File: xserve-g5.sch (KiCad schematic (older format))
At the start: 17 parts, among them J1 SATA_Backplane_PWR, J10 FAN5_PWM, J11 FAN6_PWM, J12 FAN7_PWM, J2 FAN_LEFT, J3 FAN_RIGHT, J4 PWR_L, J5 PWR_R, J6 FAN1_PWM, J7 FAN2_PWM, J8 FAN3_PWM, J9 FAN4_PWM

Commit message: updates
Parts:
- added J13: Front Panel, Connector_PinHeader_1.27mm:PinHeader_2x17_P1.27mm_Vertical, symbol Connector_Generic:Conn_02x17_Odd_Even
- added U1: WeMos_D1_mini, Module:WEMOS_D1_mini_light, symbol MCU_Module:WeMos_D1_mini
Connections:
- net +5V: now also J13.26 (Pin_26), J13.28 (Pin_28), J13.30 (Pin_30), J13.32 (Pin_32), J13.34 (Pin_34), U1.9 (5V)
- net GND: now also J13.1 (Pin_1), J13.11 (Pin_11), J13.17 (Pin_17), J13.25 (Pin_25), J13.27 (Pin_27), J13.29 (Pin_29), J13.31 (Pin_31), J13.33 (Pin_33), J13.7 (Pin_7), U1.10 (GND)
- new net +3V3: U1.8 (3V3)
- new net CLED_RCLK: J13.10 (Pin_10)
- new net CLED_SER: J13.12 (Pin_12)
- new net CLED_SRCLK: J13.8 (Pin_8)
- new net CLED_SRCLR_n: J13.13 (Pin_13)
- new net CLED_VCC: J13.4 (Pin_4)
- new net LANA_LED: J13.19 (Pin_19)
- new net LANB_LED: J13.18 (Pin_18)
- new net PWR_LED: J13.5 (Pin_5)
- new net PWR_SW: J13.3 (Pin_3)
- new net Q19: J13.2 (Pin_2)
- new net SRVID_LED: J13.15 (Pin_15)
- new net SRVID_SW: J13.6 (Pin_6)
- new net U6_??: J13.20 (Pin_20)
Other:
- note added: "Guessed"
- note added: "apply GND"
- note added: "apply Voltage"
- note added: "to GND"
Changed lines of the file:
@@
 Wire Notes Line
 	4850 550  550  550
+$Comp
+L power:GND #PWR0103
+U 1 1 5F39D41C
+P 6700 2300
+F 0 "#PWR0103" H 6700 2050 50  0001 C CNN
+F 1 "GND" H 6705 2127 50  0000 C CNN
+F 2 "" H 6700 2300 50  0001 C CNN
+F 3 "" H 6700 2300 50  0001 C CNN
+	1    6700 2300
+	0    1    1    0
+$EndComp
+$Comp
+L Connector_Generic:Conn_02x17_Odd_Even J13
+U 1 1 5F3A8D6B
+P 7000 1700
+F 0 "J13" H 7050 2717 50  0000 C CNN
+F 1 "Front Panel" H 7050 2626 50  0000 C CNN
+F 2 "Connector_PinHeader_1.27mm:PinHeader_2x17_P1.27mm_Vertical" H 7000 1700 50  0001 C CNN
+F 3 "~" H 7000 1700 50  0001 C CNN
+F 4 "Harwin M50-3551742" H 7000 1700 50  0001 C CNN "Part"
+	1    7000 1700
+	1    0    0    -1
+$EndComp
+$Comp
+L MCU_Module:WeMos_D1_mini U1
+U 1 1 5F3B1E0C
+P 9600 1650
+F 0 "U1" H 9600 669 50  0000 C CNN
+F 1 "WeMos_D1_mini" H 9600 760 50  0000 C CNN
+F 2 "Module:WEMOS_D1_mini_light" H 9600 500 50  0001 C CNN
+F 3 "https://wiki.wemos.cc/products:d1:d1_mini#documentation" H 7750 500 50  0001 C CNN
+	1    9600 1650
+	-1   0    0    1
+$EndComp
+$Comp
+L power:GND #PWR0121
+U 1 1 5F3C5F82
+P 9600 850
+F 0 "#PWR0121" H 9600 600 50  0001 C CNN
+F 1 "GND" H 9605 677 50  0000 C CNN
+F 2 "" H 9600 850 50  0001 C CNN
+F 3 "" H 9600 850 50  0001 C CNN
+	1    9600 850
+	0    -1   -1   0
+$EndComp
+Text GLabel 6800 1100 0    50   Input ~ 0
+PWR_LED
+Wire Wire Line
+	6800 2100 6800 2200
+Wire Wire Line
+	6800 2200 6800 2300
+Connection ~ 6800 2200
+Wire Wire Line
+	6800 2300 6800 2400
+Connection ~ 6800 2300
+Connection ~ 6800 2400
+Wire Wire Line
+	6800 2400 6800 2500
+Wire Wire Line
+	6700 2300 6800 2300
+Text GLabel 7300 1400 2    50   Input ~ 0
+CLED_SER
+Text GLabel 7300 1000 2    50   Input ~ 0
+CLED_VCC
+$Comp
+L power:GND #PWR?
+U 1 1 5F3CE2DC
+P 6800 900
+F 0 "#PWR?" H 6800 650 50  0001 C CNN
+F 1 "GND" H 6805 727 50  0000 C CNN
+F 2 "" H 6800 900 50  0001 C CNN
+F 3 "" H 6800 900 50  0001 C CNN
+	1    6800 900
+	0    1    1    0
+$EndComp
+$Comp
+L power:GND #PWR?
+U 1 1 5F3CEC27
+P 6800 1200
+F 0 "#PWR?" H 6800 950 50  0001 C CNN
+F 1 "GND" H 6805 1027 50  0000 C CNN
+F 2 "" H 6800 1200 50  0001 C CNN
+F 3 "" H 6800 1200 50  0001 C CNN
+	1    6800 1200
+	0    1    1    0
+$EndComp
+$Comp
+L power:GND #PWR?
+U 1 1 5F3CEED3
+P 6800 1400
+F 0 "#PWR?" H 6800 1150 50  0001 C CNN
+F 1 "GND" H 6805 1227 50  0000 C CNN
+F 2 "" H 6800 1400 50  0001 C CNN
+F 3 "" H 6800 1400 50  0001 C CNN
+	1    6800 1400
+	0    1    1    0
+$EndComp
+$Comp
+L power:GND #PWR?
+U 1 1 5F3CF6D7
+P 6800 1700
+F 0 "#PWR?" H 6800 1450 50  0001 C CNN
+F 1 "GND" H 6805 1527 50  0000 C CNN
+F 2 "" H 6800 1700 50  0001 C CNN
+F 3 "" H 6800 1700 50  0001 C CNN
+	1    6800 1700
+	0    1    1    0
+$EndComp
+Text GLabel 7300 1300 2    50   Input ~ 0
+CLED_RCLK
+Text GLabel 7300 1200 2    50   Input ~ 0
+CLED_SRCLK
+Text GLabel 6800 1500 0    50   Input ~ 0
+CLED_SRCLR_n
+Wire Wire Line
+	7300 2100 7300 2200
+Wire Wire Line
+	7300 2200 7300 2300
+Connection ~ 7300 2200
+Wire Wire Line
+	7300 2300 7300 2400
+Connection ~ 7300 2300
+Wire Wire Line
+	7300 2400 7300 2500
+Connection ~ 7300 2400
+$Comp
+L power:+5V #PWR?
+U 1 1 5F3D4B59
+P 7300 2300
+F 0 "#PWR?" H 7300 2150 50  0001 C CNN
+F 1 "+5V" V 7315 2428 50  0000 L CNN
+F 2 "" H 7300 2300 50  0001 C CNN
+F 3 "" H 7300 2300 50  0001 C CNN
+	1    7300 2300
+	0    1    1    0
+$EndComp
+$Comp
+L power:+5V #PWR?
+U 1 1 5F3D5D72
+P 9700 2450
+F 0 "#PWR?" H 9700 2300 50  0001 C CNN
+F 1 "+5V" H 9715 2623 50  0000 C CNN
+F 2 "" H 9700 2450 50  0001 C CNN
+F 3 "" H 9700 2450 50  0001 C CNN
+	1    9700 2450
+	-1   0    0    1
+$EndComp
+Text Notes 7600 2350 0    50   ~ 0
+Guessed
+Text GLabel 6800 1000 0    50   Input ~ 0
+PWR_SW
+Text Notes 6150 1050 0    50   ~ 0
+to GND
+Text GLabel 7300 1100 2    50   Input ~ 0
+SRVID_SW
+Text Notes 7750 1100 0    50   ~ 0
+to GND
+Text GLabel 6800 1600 0    50   Input ~ 0
+SRVID_LED
+Text Notes 5900 1150 0    50   ~ 0
+apply Voltage
+Text Notes 5950 1650 0    50   ~ 0
+apply GND
+Text GLabel 6800 1800 0    50   Input ~ 0
+LANA_LED
+Text GLabel 7300 1700 2    50   Input ~ 0
+LANB_LED
+$Comp
+L power:+3.3V #PWR?
+U 1 1 5F3DAB15
+P 9500 2450
+F 0 "#PWR?" H 9500 2300 50  0001 C CNN
+F 1 "+3.3V" H 9515 2623 50  0000 C CNN
+F 2 "" H 9500 2450 50  0001 C CNN
+F 3 "" H 9500 2450 50  0001 C CNN
+	1    9500 2450
+	-1   0    0    1
+$EndComp
+Text GLabel 7300 900  2    50   Input ~ 0
+Q19
+Text GLabel 7300 1800 2    50   Input ~ 0
+U6_??
 $EndSCHEMATC

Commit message: update
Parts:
- added J14: SYSTEM_PINS, Connector_PinHeader_2.54mm:PinHeader_1x06_P2.54mm_Horizontal, symbol Connector_Generic:Conn_01x06
- added J15: CLED_VCC, Connector_PinHeader_2.54mm:PinHeader_1x03_P2.54mm_Vertical, symbol Connector_Generic:Conn_01x03
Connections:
- net CLED_VCC is gone; now on net CLED_SRCLR_n: J13.4 (Pin_4)
- net U6_?? is gone; now on net CLED_SRCLR_n: J13.20 (Pin_20)
- net +12V: no longer J3.10 (Pin_10), J3.8 (Pin_8), J5.1 (Pin_1)
- net +3V3: now also J15.1 (Pin_1)
- net +5V: no longer J13.26 (Pin_26), J13.28 (Pin_28), J13.30 (Pin_30), J13.32 (Pin_32), J13.34 (Pin_34), U1.9 (5V)
- net CLED_RCLK: now also U1.6 (MOSI/D7)
- net CLED_SER: now also U1.5 (MISO/D6)
- net CLED_SRCLK: now also U1.4 (SCK/D5)
- net CLED_SRCLR_n: now also J13.14 (Pin_14), J13.9 (Pin_9), J15.2 (Pin_2)
- net LANA_LED: now also J14.5 (Pin_5)
- net LANB_LED: now also J14.6 (Pin_6)
- net PWR_LED: now also J14.1 (Pin_1)
- net PWR_SW: now also J14.2 (Pin_2)
- net SRVID_LED: now also J14.3 (Pin_3)
- net SRVID_SW: now also J14.4 (Pin_4)
- net Q13: now reaches J13.22 (Pin_22)
- new net +12VA: J3.10 (Pin_10), J3.8 (Pin_8), J5.1 (Pin_1)
- new net +5VA: J13.26 (Pin_26), J13.28 (Pin_28), J13.30 (Pin_30), J13.32 (Pin_32), J13.34 (Pin_34), J15.3 (Pin_3), U1.9 (5V)
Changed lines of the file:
@@
 Wire Wire Line
 	2550 1150 2250 1150
-$Comp
-L power:+12V #PWR0110
-U 1 1 5F376BAA
-P 2500 3600
-F 0 "#PWR0110" H 2500 3450 50  0001 C CNN
-F 1 "+12V" H 2515 3773 50  0000 C CNN
-F 2 "" H 2500 3600 50  0001 C CNN
-F 3 "" H 2500 3600 50  0001 C CNN
-	1    2500 3600
-	0    1    1    0
-$EndComp
 Text GLabel 2100 3400 2    50   Input ~ 0
 TACH5
@@
 Wire Wire Line
 	2500 3600 2100 3600
-Connection ~ 2500 3600
 $Comp
 L Connector_Generic:Conn_01x04 J6
@@
 PWM7
 $Comp
-L power:+12V #PWR0113
-U 1 1 5F39C714
-P 750 4450
-F 0 "#PWR0113" H 750 4300 50  0001 C CNN
-F 1 "+12V" H 765 4623 50  0000 C CNN
-F 2 "" H 750 4450 50  0001 C CNN
-F 3 "" H 750 4450 50  0001 C CNN
-	1    750  4450
-	-1   0    0    1
-$EndComp
-$Comp
 L power:GND #PWR0114
 U 1 1 5F39CCFD
@@
 	1    0    0    -1
 $EndComp
-$Comp
-L MCU_Module:WeMos_D1_mini U1
-U 1 1 5F3B1E0C
-P 9600 1650
-F 0 "U1" H 9600 669 50  0000 C CNN
-F 1 "WeMos_D1_mini" H 9600 760 50  0000 C CNN
-F 2 "Module:WEMOS_D1_mini_light" H 9600 500 50  0001 C CNN
-F 3 "https://wiki.wemos.cc/products:d1:d1_mini#documentation" H 7750 500 50  0001 C CNN
-	1    9600 1650
-	-1   0    0    1
-$EndComp
-$Comp
-L power:GND #PWR0121
-U 1 1 5F3C5F82
-P 9600 850
-F 0 "#PWR0121" H 9600 600 50  0001 C CNN
-F 1 "GND" H 9605 677 50  0000 C CNN
-F 2 "" H 9600 850 50  0001 C CNN
-F 3 "" H 9600 850 50  0001 C CNN
-	1    9600 850
-	0    -1   -1   0
-$EndComp
 Text GLabel 6800 1100 0    50   Input ~ 0
 PWR_LED
@@
 CLED_VCC
 $Comp
-L power:GND #PWR?
+L power:GND #PWR0122
 U 1 1 5F3CE2DC
 P 6800 900
-F 0 "#PWR?" H 6800 650 50  0001 C CNN
+F 0 "#PWR0122" H 6800 650 50  0001 C CNN
 F 1 "GND" H 6805 727 50  0000 C CNN
 F 2 "" H 6800 900 50  0001 C CNN
@@
 $EndComp
 $Comp
-L power:GND #PWR?
+L power:GND #PWR0123
 U 1 1 5F3CEC27
 P 6800 1200
-F 0 "#PWR?" H 6800 950 50  0001 C CNN
+F 0 "#PWR0123" H 6800 950 50  0001 C CNN
 F 1 "GND" H 6805 1027 50  0000 C CNN
 F 2 "" H 6800 1200 50  0001 C CNN
@@
 $EndComp
 $Comp
-L power:GND #PWR?
+L power:GND #PWR0124
 U 1 1 5F3CEED3
 P 6800 1400
-F 0 "#PWR?" H 6800 1150 50  0001 C CNN
+F 0 "#PWR0124" H 6800 1150 50  0001 C CNN
 F 1 "GND" H 6805 1227 50  0000 C CNN
 F 2 "" H 6800 1400 50  0001 C CNN
@@
 $EndComp
 $Comp
-L power:GND #PWR?
+L power:GND #PWR0125
 U 1 1 5F3CF6D7
 P 6800 1700
-F 0 "#PWR?" H 6800 1450 50  0001 C CNN
+F 0 "#PWR0125" H 6800 1450 50  0001 C CNN
 F 1 "GND" H 6805 1527 50  0000 C CNN
 F 2 "" H 6800 1700 50  0001 C CNN
@@
 	7300 2400 7300 2500
 Connection ~ 7300 2400
-$Comp
-L power:+5V #PWR?
-U 1 1 5F3D4B59
-P 7300 2300
-F 0 "#PWR?" H 7300 2150 50  0001 C CNN
-F 1 "+5V" V 7315 2428 50  0000 L CNN
-F 2 "" H 7300 2300 50  0001 C CNN
-F 3 "" H 7300 2300 50  0001 C CNN
-	1    7300 2300
-	0    1    1    0
-$EndComp
-$Comp
-L power:+5V #PWR?
-U 1 1 5F3D5D72
-P 9700 2450
-F 0 "#PWR?" H 9700 2300 50  0001 C CNN
-F 1 "+5V" H 9715 2623 50  0000 C CNN
-F 2 "" H 9700 2450 50  0001 C CNN
-F 3 "" H 9700 2450 50  0001 C CNN
-	1    9700 2450
-	-1   0    0    1
-$EndComp
 Text Notes 7600 2350 0    50   ~ 0
 Guessed
@@
 Text GLabel 7300 1700 2    50   Input ~ 0
 LANB_LED
-$Comp
-L power:+3.3V #PWR?
+Text GLabel 7300 900  2    50   Input ~ 0
+Q19
+Text GLabel 7300 1900 2    50   Input ~ 0
+Q13
+Text GLabel 7300 1500 2    50   Input ~ 0
+CLED_VCC
+Text GLabel 7300 1800 2    50   Input ~ 0
+CLED_VCC
+Text GLabel 6800 1300 0    50   Input ~ 0
+CLED_VCC
+Text GLabel 5050 1000 3    50   Input ~ 0
+PWR_LED
+Text GLabel 5150 1000 3    50   Input ~ 0
+PWR_SW
+Text GLabel 5250 1000 3    50   Input ~ 0
+SRVID_LED
+Text GLabel 5450 1000 3    50   Input ~ 0
+LANA_LED
+Text GLabel 5550 1000 3    50   Input ~ 0
+LANB_LED
+$Comp
+L Connector_Generic:Conn_01x06 J14
+U 1 1 5F3CC5EE
+P 5250 800
+F 0 "J14" V 5214 412 50  0000 R CNN
+F 1 "SYSTEM_PINS" V 5123 412 50  0000 R CNN
+F 2 "Connector_PinHeader_2.54mm:PinHeader_1x06_P2.54mm_Horizontal" H 5250 800 50  0001 C CNN
+F 3 "~" H 5250 800 50  0001 C CNN
+	1    5250 800
+	0    -1   -1   0
+$EndComp
+Text GLabel 5350 1000 3    50   Input ~ 0
+SRVID_SW
+$Comp
+L power:+3.3V #PWR0128
 U 1 1 5F3DAB15
 P 9500 2450
-F 0 "#PWR?" H 9500 2300 50  0001 C CNN
+F 0 "#PWR0128" H 9500 2300 50  0001 C CNN
 F 1 "+3.3V" H 9515 2623 50  0000 C CNN
 F 2 "" H 9500 2450 50  0001 C CNN
@@
 	-1   0    0    1
 $EndComp
-Text GLabel 7300 900  2    50   Input ~ 0
-Q19
-Text GLabel 7300 1800 2    50   Input ~ 0
-U6_??
+$Comp
+L power:GND #PWR0121
+U 1 1 5F3C5F82
+P 9600 850
+F 0 "#PWR0121" H 9600 600 50  0001 C CNN
+F 1 "GND" H 9605 677 50  0000 C CNN
+F 2 "" H 9600 850 50  0001 C CNN
+F 3 "" H 9600 850 50  0001 C CNN
+	1    9600 850
+	0    -1   -1   0
+$EndComp
+$Comp
+L MCU_Module:WeMos_D1_mini U1
+U 1 1 5F3B1E0C
+P 9600 1650
+F 0 "U1" H 9600 669 50  0000 C CNN
+F 1 "WeMos_D1_mini" H 9600 760 50  0000 C CNN
+F 2 "Module:WEMOS_D1_mini_light" H 9600 500 50  0001 C CNN
+F 3 "https://wiki.wemos.cc/products:d1:d1_mini#documentation" H 7750 500 50  0001 C CNN
+	1    9600 1650
+	-1   0    0    1
+$EndComp
+$Comp
+L power:+3.3V #PWR0129
+U 1 1 5F4662CF
+P 8350 1050
+F 0 "#PWR0129" H 8350 900 50  0001 C CNN
+F 1 "+3.3V" H 8365 1223 50  0000 C CNN
+F 2 "" H 8350 1050 50  0001 C CNN
+F 3 "" H 8350 1050 50  0001 C CNN
+	1    8350 1050
+	0    -1   -1   0
+$EndComp
+Text GLabel 8350 1250 0    50   Input ~ 0
+CLED_VCC
+$Comp
+L Connector_Generic:Conn_01x03 J15
+U 1 1 5F467B70
+P 8450 850
+F 0 "J15" V 8414 662 50  0000 R CNN
+F 1 "CLED_VCC" V 8323 662 50  0000 R CNN
+F 2 "Connector_PinHeader_2.54mm:PinHeader_1x03_P2.54mm_Vertical" H 8450 850 50  0001 C CNN
+F 3 "~" H 8450 850 50  0001 C CNN
+	1    8450 850
+	0    -1   -1   0
+$EndComp
+Text GLabel 9200 1450 0    50   Input ~ 0
+CLED_SER
+Text GLabel 9200 1350 0    50   Input ~ 0
+CLED_RCLK
+Text GLabel 9200 1550 0    50   Input ~ 0
+CLED_SRCLK
+Text GLabel 8450 1350 0    50   Input ~ 0
+CLED_SRCLR_n
+Wire Wire Line
+	8450 1050 8450 1250
+Wire Wire Line
+	8450 1250 8350 1250
+Wire Wire Line
+	8450 1250 8450 1350
+Connection ~ 8450 1250
+$Comp
+L power:+5VA #PWR0126
+U 1 1 5F47D20F
+P 9700 2450
+F 0 "#PWR0126" H 9700 2300 50  0001 C CNN
+F 1 "+5VA" H 9715 2623 50  0000 C CNN
+F 2 "" H 9700 2450 50  0001 C CNN
+F 3 "" H 9700 2450 50  0001 C CNN
+	1    9700 2450
+	-1   0    0    1
+$EndComp
+$Comp
+L power:+5VA #PWR0127
+U 1 1 5F47E5E1
+P 8550 1050
+F 0 "#PWR0127" H 8550 900 50  0001 C CNN
+F 1 "+5VA" V 8565 1178 50  0000 L CNN
+F 2 "" H 8550 1050 50  0001 C CNN
+F 3 "" H 8550 1050 50  0001 C CNN
+	1    8550 1050
+	0    1    1    0
+$EndComp
+$Comp
+L power:+5VA #PWR0130
+U 1 1 5F480819
+P 7300 2300
+F 0 "#PWR0130" H 7300 2150 50  0001 C CNN
+F 1 "+5VA" V 7315 2428 50  0000 L CNN
+F 2 "" H 7300 2300 50  0001 C CNN
+F 3 "" H 7300 2300 50  0001 C CNN
+	1    7300 2300
+	0    1    1    0
+$EndComp
+$Comp
+L power:+12VA #PWR?
+U 1 1 5F49C765
+P 750 4450
+F 0 "#PWR?" H 750 4300 50  0001 C CNN
+F 1 "+12VA" H 765 4623 50  0000 C CNN
+F 2 "" H 750 4450 50  0001 C CNN
+F 3 "" H 750 4450 50  0001 C CNN
+	1    750  4450
+	-1   0    0    1
+$EndComp
+$Comp
+L power:+12VA #PWR?
+U 1 1 5F49E0B2
+P 2500 3600
+F 0 "#PWR?" H 2500 3450 50  0001 C CNN
+F 1 "+12VA" V 2515 3728 50  0000 L CNN
+F 2 "" H 2500 3600 50  0001 C CNN
+F 3 "" H 2500 3600 50  0001 C CNN
+	1    2500 3600
+	0    1    1    0
+$EndComp
+Connection ~ 2500 3600
 $EndSCHEMATC

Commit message: update
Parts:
- added J16: CLED, Connector_PinHeader_2.54mm:PinHeader_1x05_P2.54mm_Horizontal, symbol Connector_Generic:Conn_01x05
- added J17: BP_SMBUS, Connector_PinHeader_2.54mm:PinHeader_1x05_P2.54mm_Horizontal, symbol Connector_Generic:Conn_01x05
- added JP6: PWM1_4, Connector_PinHeader_2.54mm:PinHeader_1x02_P2.54mm_Vertical, symbol Device:Jumper
- J14: footprint Connector_PinHeader_2.54mm:PinHeader_1x06_P2.54mm_Horizontal -> Connector_PinHeader_2.54mm:PinHeader_1x07_P2.54mm_Horizontal; symbol Connector_Generic:Conn_01x06 -> Connector_Generic:Conn_01x07
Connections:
- net CLED_RCLK: now also J16.4 (Pin_4)
- net CLED_SER: now also J16.5 (Pin_5)
- net CLED_SRCLK: now also J16.3 (Pin_3)
- net CLED_SRCLR_n: now also J16.2 (Pin_2), JP6.2; no longer J13.14 (Pin_14), J13.20 (Pin_20), J13.4 (Pin_4), J13.9 (Pin_9), J15.2 (Pin_2)
- net GND: now also J14.7 (Pin_7), J17.1 (Pin_1)
- net PWM1: no longer JP2.2, JP3.2
- net PWM2: now also JP2.2
- net PWM3: now also JP3.2
- net PWM5: no longer JP5.2
- net PWM6: now also JP5.2
- net SMBUS_SCL: now reaches J1.1 (Pin_1)
- net SMBUS_SCL: now also J17.3 (Pin_3)
- net SMBUS_SDA: now reaches J1.7 (Pin_7)
- net SMBUS_SDA: now also J17.4 (Pin_4)
- net BP_UNKN: now reaches J1.8 (Pin_8)
- net BP_UNKN: now also J17.5 (Pin_5)
- net SMBUS_VCC: now reaches J1.9 (Pin_9)
- net SMBUS_VCC: now also J17.2 (Pin_2)
- new net CLED_VCC: J13.14 (Pin_14), J13.20 (Pin_20), J13.4 (Pin_4), J13.9 (Pin_9), J15.2 (Pin_2), J16.1 (Pin_1), JP6.1
- no-connect marks 12 -> 8
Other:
- note removed: "3.3V ??"
- note removed: "??"
- moved on the sheet: J2, U1

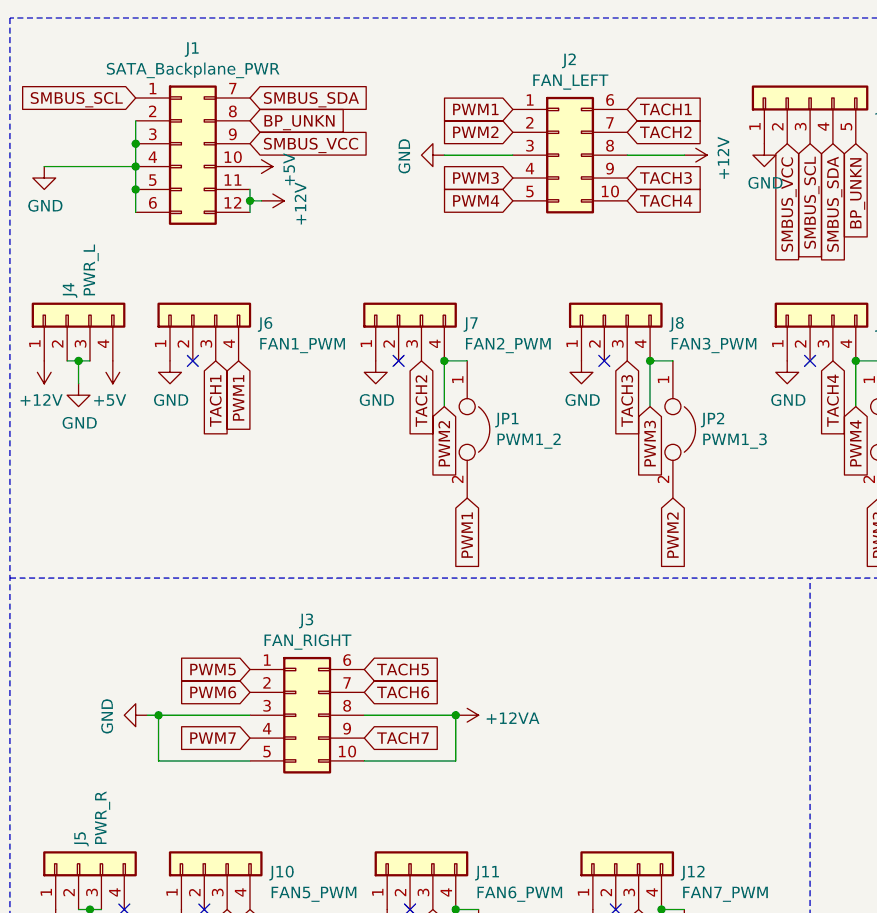
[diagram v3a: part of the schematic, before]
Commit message: Switch pwm and tacho pins...
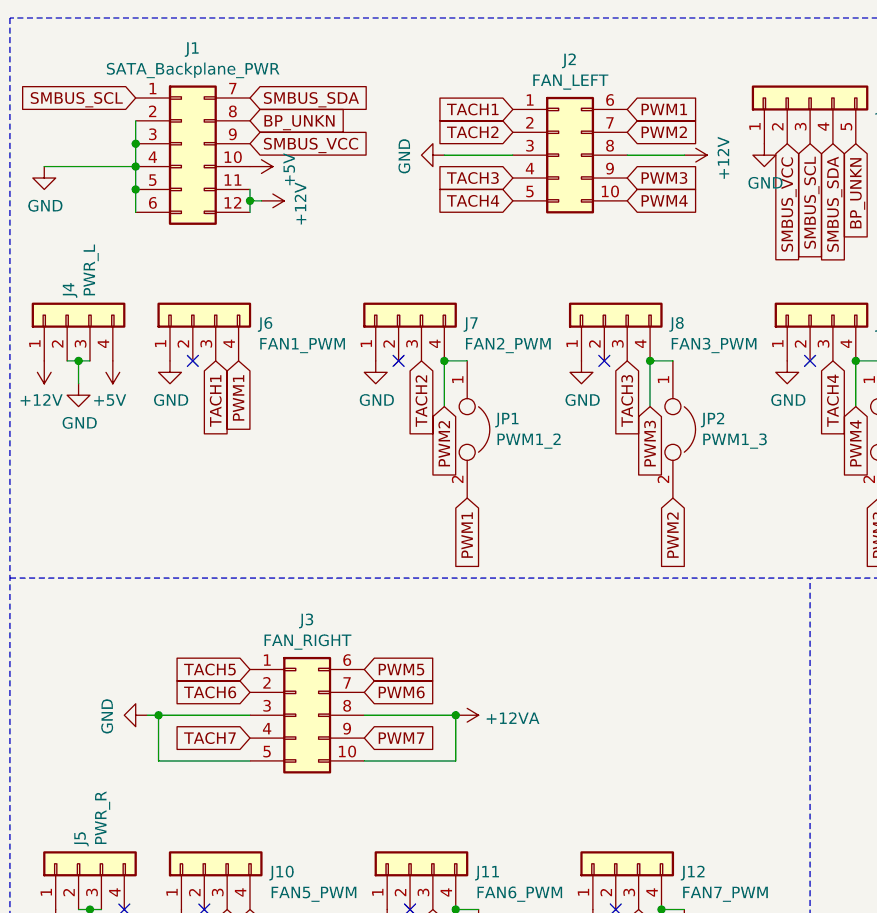
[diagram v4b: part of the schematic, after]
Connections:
- net PWM1: now also J2.6 (Pin_6); no longer J2.1 (Pin_1)
- net PWM2: now also J2.7 (Pin_7); no longer J2.2 (Pin_2)
- net PWM3: now also J2.9 (Pin_9); no longer J2.4 (Pin_4)
- net PWM4: now also J2.10 (Pin_10); no longer J2.5 (Pin_5)
- net PWM5: now also J3.6 (Pin_6); no longer J3.1 (Pin_1)
- net PWM6: now also J3.7 (Pin_7); no longer J3.2 (Pin_2)
- net PWM7: now also J3.9 (Pin_9); no longer J3.4 (Pin_4)
- net TACH1: now also J2.1 (Pin_1); no longer J2.6 (Pin_6)
- net TACH2: now also J2.2 (Pin_2); no longer J2.7 (Pin_7)
- net TACH3: now also J2.4 (Pin_4); no longer J2.9 (Pin_9)
- net TACH4: now also J2.5 (Pin_5); no longer J2.10 (Pin_10)
- net TACH5: now also J3.1 (Pin_1); no longer J3.6 (Pin_6)
- net TACH6: now also J3.2 (Pin_2); no longer J3.7 (Pin_7)
- net TACH7: now also J3.4 (Pin_4); no longer J3.9 (Pin_9)
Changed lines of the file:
@@
 	0    1    1    0
 $EndComp
-Text GLabel 3250 950  2    50   Input ~ 0
+Text GLabel 2750 950  0    50   Input ~ 0
 TACH1
-Text GLabel 3250 1050 2    50   Input ~ 0
+Text GLabel 2750 1050 0    50   Input ~ 0
 TACH2
-Text GLabel 3250 1250 2    50   Input ~ 0
+Text GLabel 2750 1250 0    50   Input ~ 0
 TACH3
-Text GLabel 3250 1350 2    50   Input ~ 0
+Text GLabel 2750 1350 0    50   Input ~ 0
 TACH4
 Wire Wire Line
@@
 Wire Wire Line
 	2750 1150 2450 1150
-Text GLabel 2100 3400 2    50   Input ~ 0
+Text GLabel 1600 3400 0    50   Input ~ 0
 TACH5
-Text GLabel 2100 3500 2    50   Input ~ 0
+Text GLabel 1600 3500 0    50   Input ~ 0
 TACH6
-Text GLabel 2100 3700 2    50   Input ~ 0
+Text GLabel 1600 3700 0    50   Input ~ 0
 TACH7
 $Comp
@@
 Text GLabel 1450 2050 3    50   Input ~ 0
 TACH1
-Text GLabel 2750 950  0    50   Input ~ 0
+Text GLabel 3250 950  2    50   Input ~ 0
 PWM1
-Text GLabel 2750 1050 0    50   Input ~ 0
+Text GLabel 3250 1050 2    50   Input ~ 0
 PWM2
-Text GLabel 2750 1250 0    50   Input ~ 0
+Text GLabel 3250 1250 2    50   Input ~ 0
 PWM3
-Text GLabel 2750 1350 0    50   Input ~ 0
+Text GLabel 3250 1350 2    50   Input ~ 0
 PWM4
-Text GLabel 1600 3400 0    50   Input ~ 0
+Text GLabel 2100 3400 2    50   Input ~ 0
 PWM5
-Text GLabel 1600 3500 0    50   Input ~ 0
+Text GLabel 2100 3500 2    50   Input ~ 0
 PWM6
-Text GLabel 1600 3700 0    50   Input ~ 0
+Text GLabel 2100 3700 2    50   Input ~ 0
 PWM7
 $Comp
